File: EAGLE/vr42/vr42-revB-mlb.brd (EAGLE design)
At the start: 70 x 30 mm, 87 parts, among them SW2 KMR2, U1 2N7002, U2 2N7002, U3 74AHCT1G125GW, U33 USB3300-EZK, X1 12MHz, X2 32.768MHz, X3 24MHz

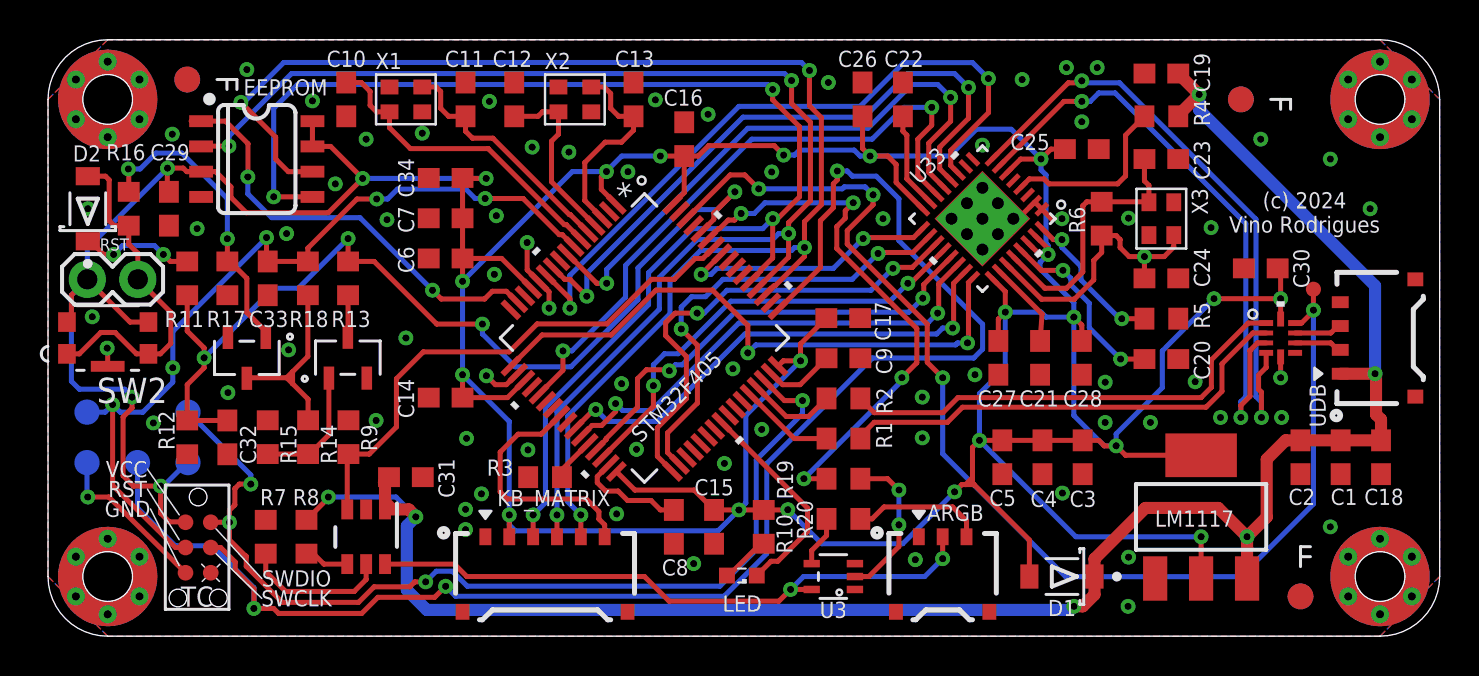
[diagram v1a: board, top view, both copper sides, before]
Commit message: fixed signal pairs
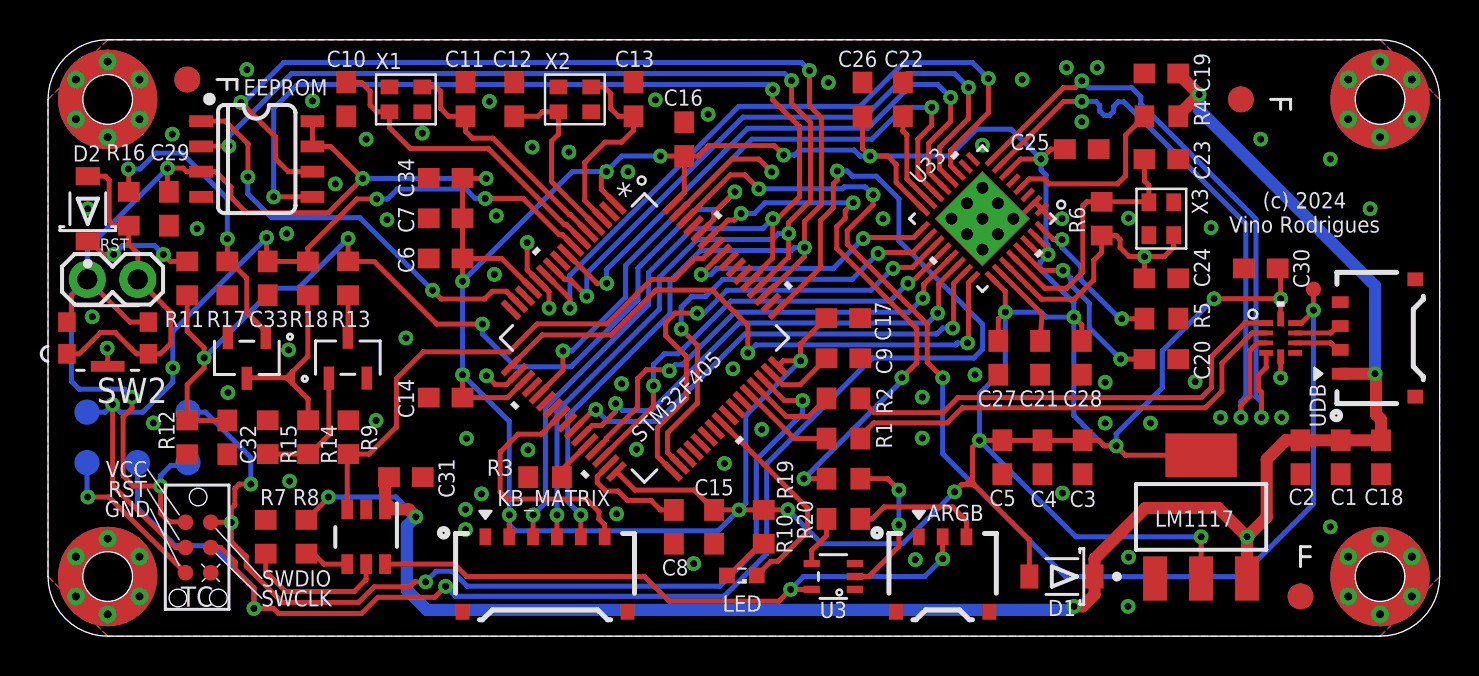
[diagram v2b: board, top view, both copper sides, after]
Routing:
- net GND: track 19.1 -> 25.1 mm, vias 70 -> 71
- net SWDIO: track 50.1 -> 50.7 mm
- net USB2_P: track 31.1 -> 31.6 mm
